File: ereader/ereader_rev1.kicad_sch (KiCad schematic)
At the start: 0 parts

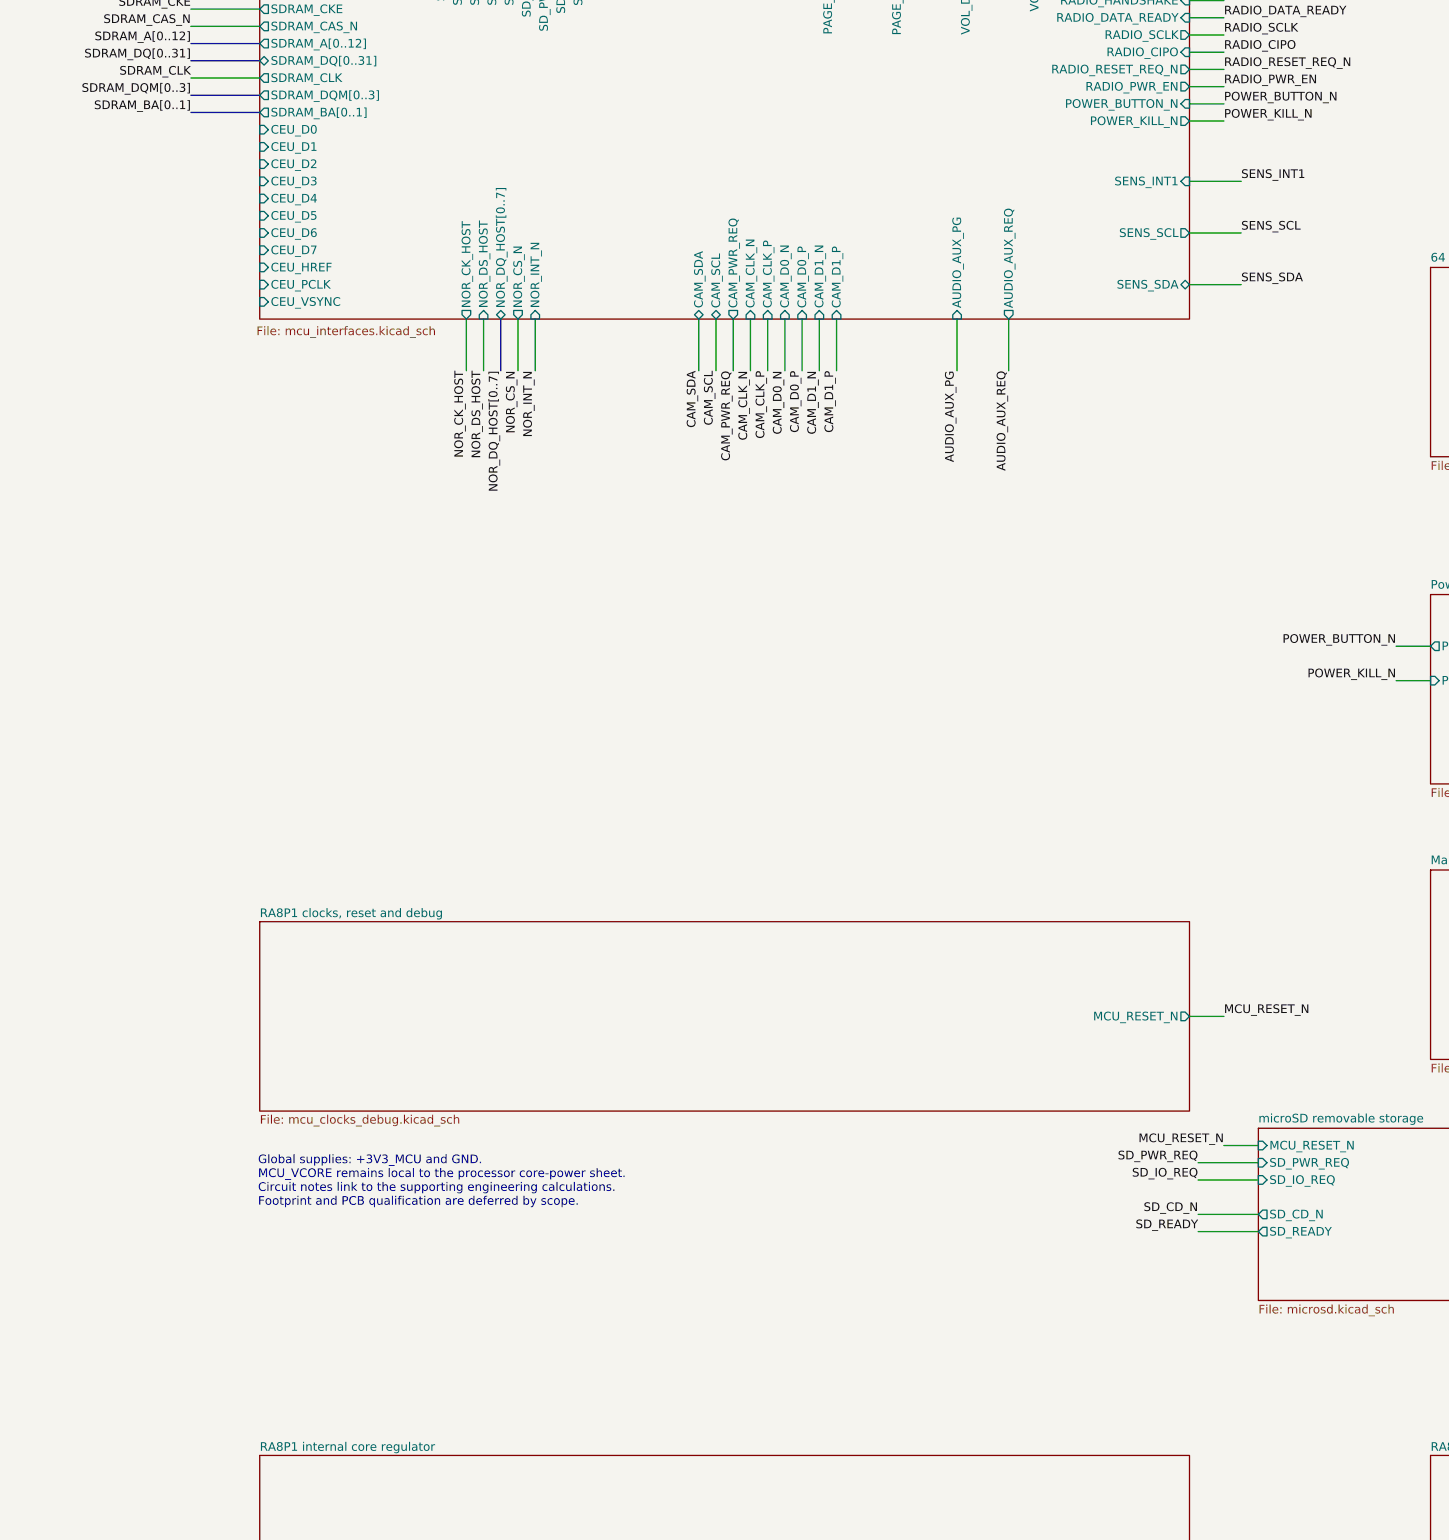
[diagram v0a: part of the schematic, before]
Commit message: Add buffered SCI4 NAND storage schematic
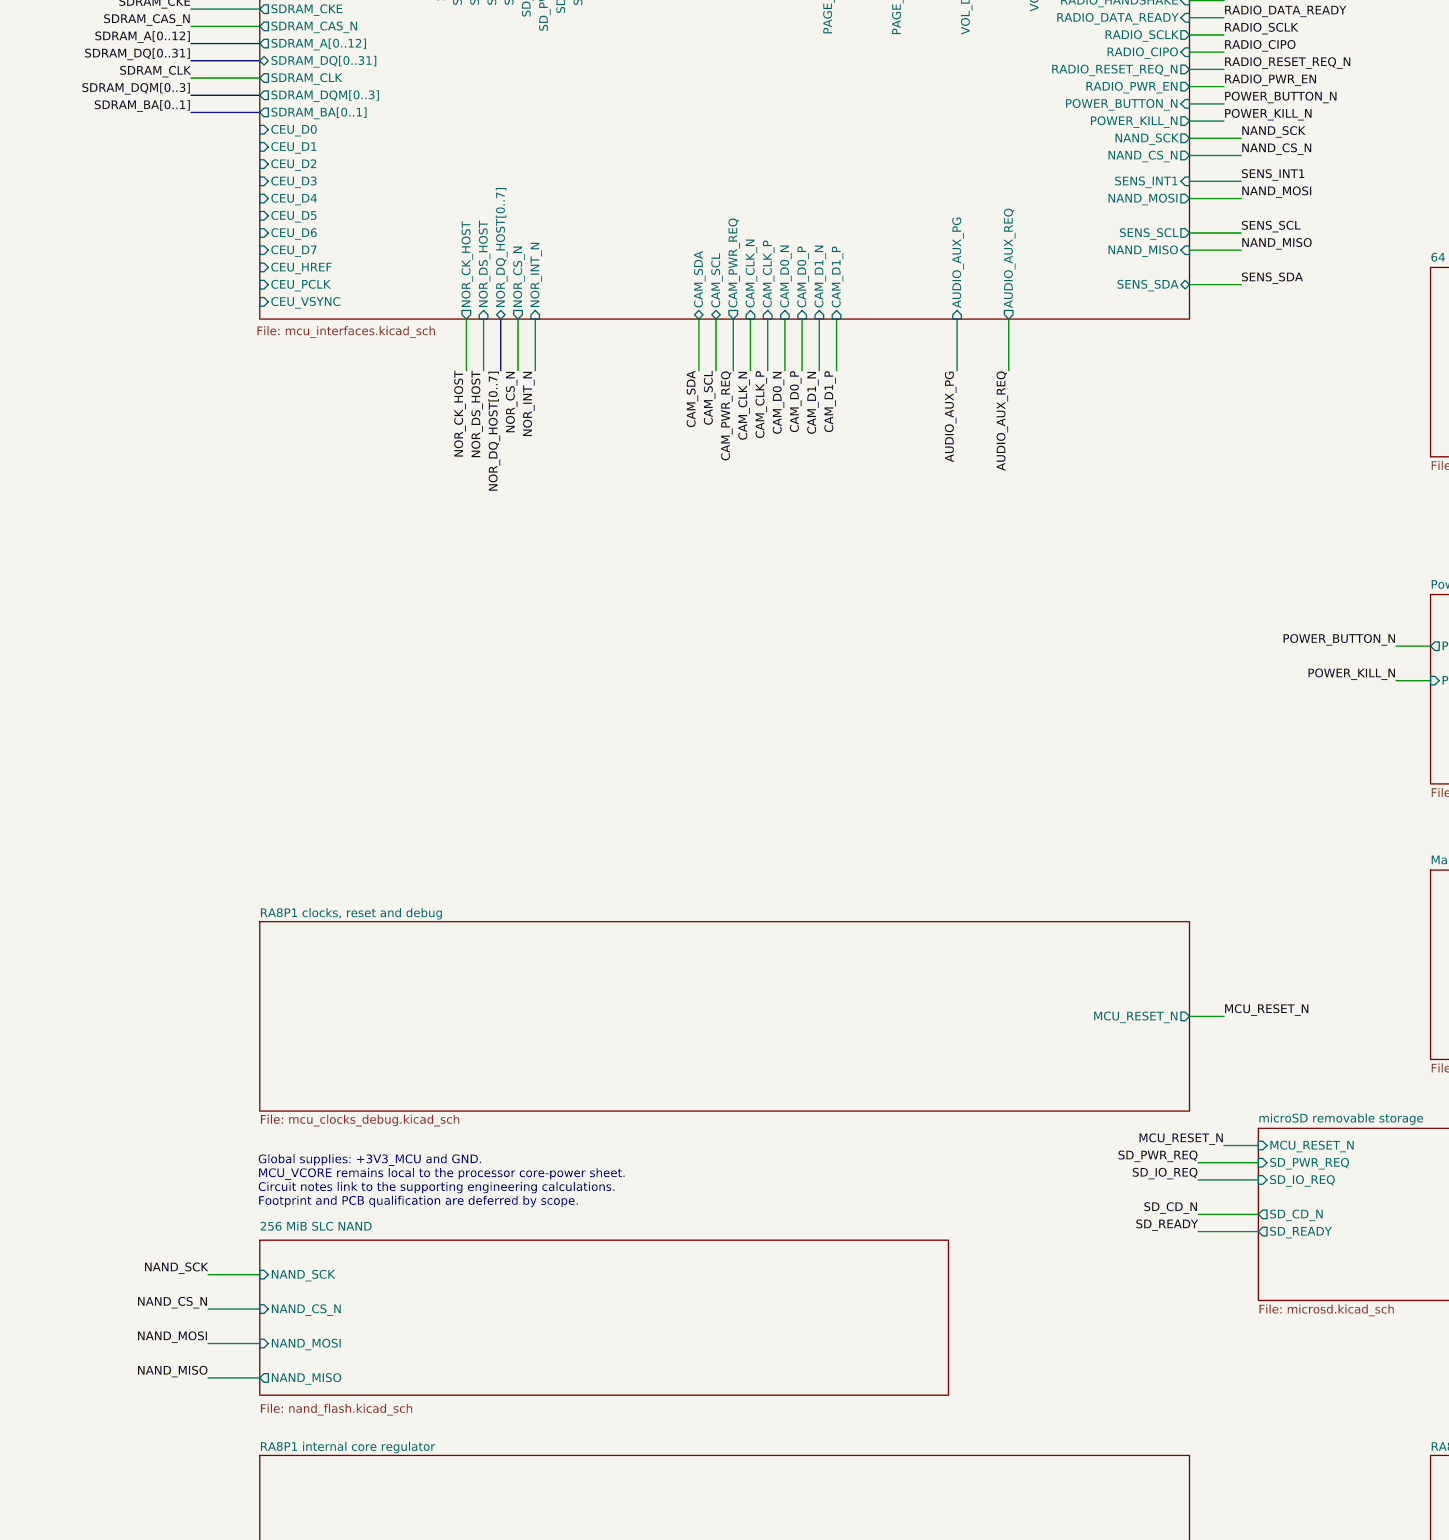
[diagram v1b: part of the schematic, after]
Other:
- added sheet 256 MiB SLC NAND (nand_flash.kicad_sch)
- sheet RA8P1 IO allocation ports: added NAND_CS_N, NAND_MISO, NAND_MOSI, NAND_SCK; removed none
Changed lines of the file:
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@@
 			)
 		)
-	)
+	(pin "NAND_SCK" output (at 199.39 106.68 0) (effects (font (size 1.27 1.27)) (justify right)))
+(pin "NAND_CS_N" output (at 199.39 109.22 0) (effects (font (size 1.27 1.27)) (justify right)))
+(pin "NAND_MOSI" output (at 199.39 115.57 0) (effects (font (size 1.27 1.27)) (justify right)))
+(pin "NAND_MISO" input (at 199.39 123.19 0) (effects (font (size 1.27 1.27)) (justify right)))
+)
 	(sheet
 		(at 209.55 252.73)
@@
 	)
 	(embedded_fonts no)
+(wire (pts (xy 199.39 106.68) (xy 207.01 106.68)) (stroke (width 0) (type default)))
+(label "NAND_SCK" (at 207.01 106.68 0) (effects (font (size 1.27 1.27)) (justify left bottom)))
+(wire (pts (xy 199.39 109.22) (xy 207.01 109.22)) (stroke (width 0) (type default)))
+(label "NAND_CS_N" (at 207.01 109.22 0) (effects (font (size 1.27 1.27)) (justify left bottom)))
+(wire (pts (xy 199.39 115.57) (xy 207.01 115.57)) (stroke (width 0) (type default)))
+(label "NAND_MOSI" (at 207.01 115.57 0) (effects (font (size 1.27 1.27)) (justify left bottom)))
+(wire (pts (xy 199.39 123.19) (xy 207.01 123.19)) (stroke (width 0) (type default)))
+(label "NAND_MISO" (at 207.01 123.19 0) (effects (font (size 1.27 1.27)) (justify left bottom)))
+(wire (pts (xy 62.23 274.32) (xy 54.61 274.32)) (stroke (width 0) (type default)))
+(label "NAND_SCK" (at 54.61 274.32 180) (effects (font (size 1.27 1.27)) (justify right bottom)))
+(wire (pts (xy 62.23 279.4) (xy 54.61 279.4)) (stroke (width 0) (type default)))
+(label "NAND_CS_N" (at 54.61 279.4 180) (effects (font (size 1.27 1.27)) (justify right bottom)))
+(wire (pts (xy 62.23 284.48) (xy 54.61 284.48)) (stroke (width 0) (type default)))
+(label "NAND_MOSI" (at 54.61 284.48 180) (effects (font (size 1.27 1.27)) (justify right bottom)))
+(wire (pts (xy 62.23 289.56) (xy 54.61 289.56)) (stroke (width 0) (type default)))
+(label "NAND_MISO" (at 54.61 289.56 180) (effects (font (size 1.27 1.27)) (justify right bottom)))
+(sheet (at 62.23 269.24) (size 101.6 22.86) (exclude_from_sim no) (in_bom yes) (on_board yes) (dnp no) (stroke (width 0.1524) (type solid)) (fill (color 0 0 0 0)) (property "Sheetname" "256 MiB SLC NAND" (at 62.23 267.97 0) (effects (font (size 1.27 1.27)) (justify left bottom)))(property "Sheetfile" "nand_flash.kicad_sch" (at 62.23 293.37 0) (effects (font (size 1.27 1.27)) (justify left top)))(pin "NAND_SCK" input (at 62.23 274.32 180) (effects (font (size 1.27 1.27)) (justify left)))(pin "NAND_CS_N" input (at 62.23 279.4 180) (effects (font (size 1.27 1.27)) (justify left)))(pin "NAND_MOSI" input (at 62.23 284.48 180) (effects (font (size 1.27 1.27)) (justify left)))(pin "NAND_MISO" output (at 62.23 289.56 180) (effects (font (size 1.27 1.27)) (justify left)))(instances (project "ereader_rev1" (path "/0586cc51-9c57-495b-a0c9-c29ba0d48166" (page "16")))))
 )

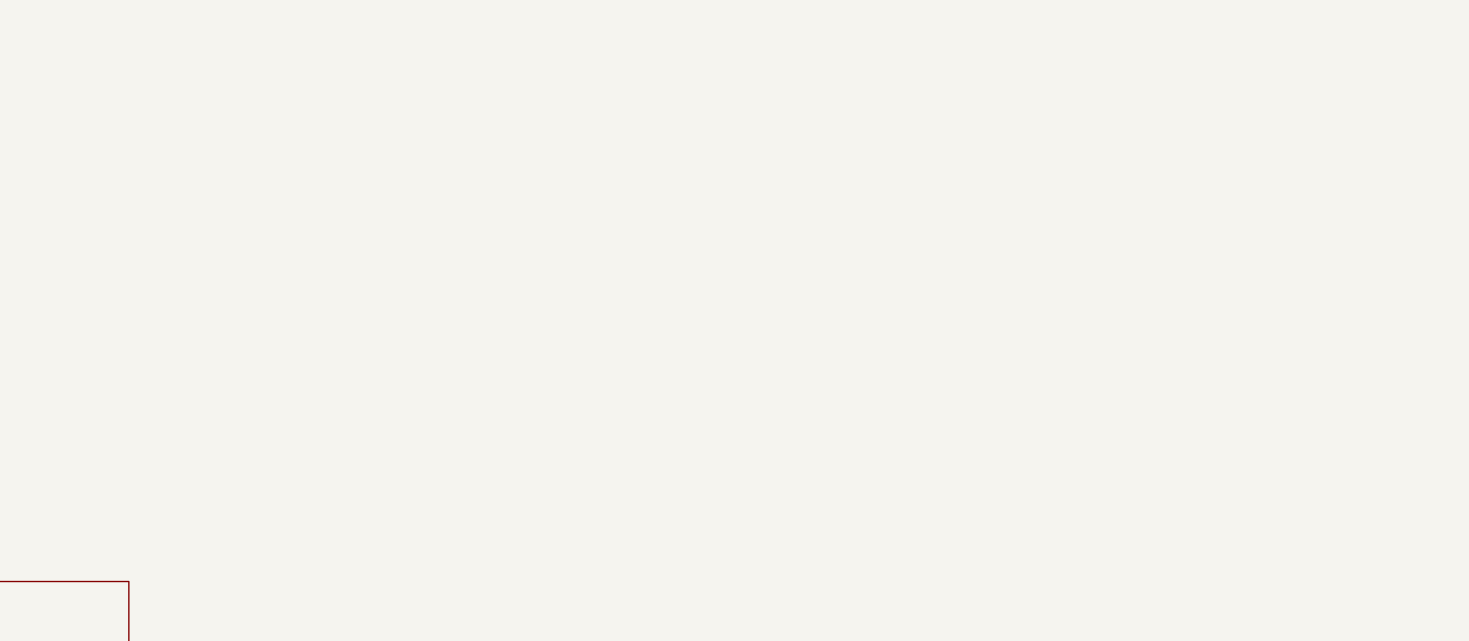
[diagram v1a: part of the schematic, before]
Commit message: Add isolated source-local AUX electrical draft and independent gates
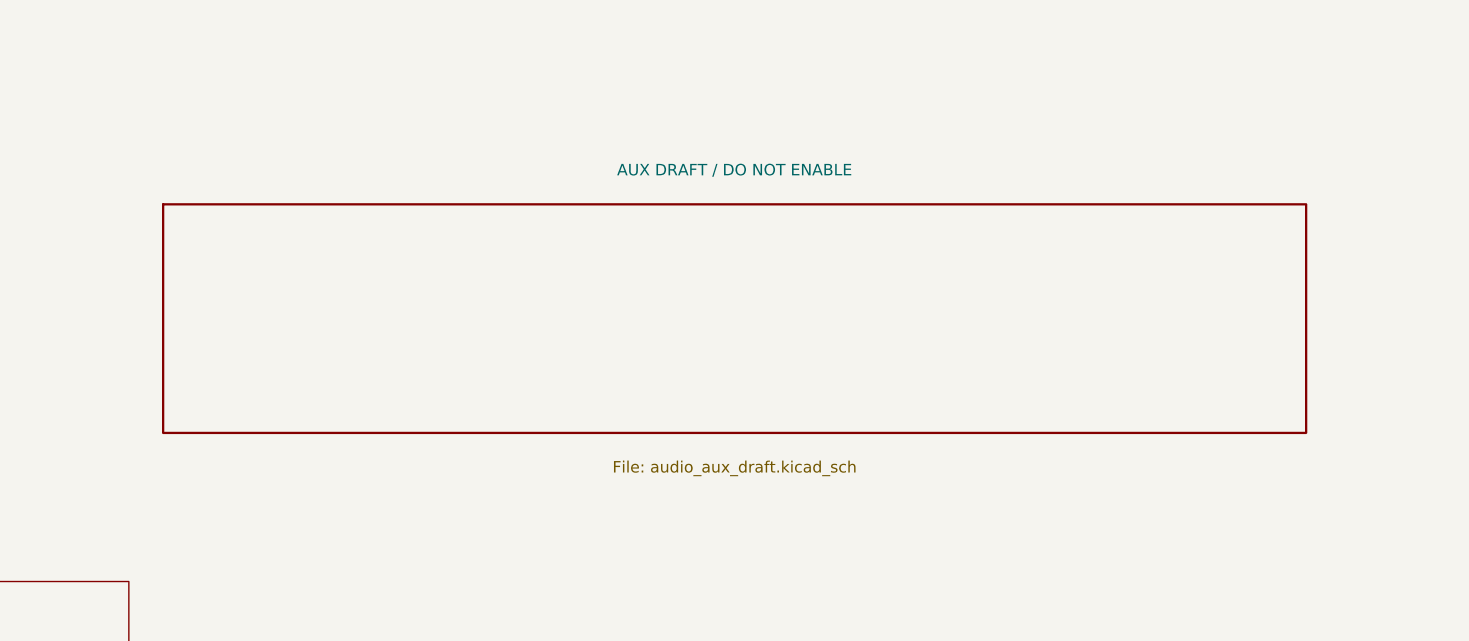
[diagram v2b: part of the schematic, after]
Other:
- added sheet AUX DRAFT / DO NOT ENABLE (audio_aux_draft.kicad_sch)
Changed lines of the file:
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@@
 (label "NAND_MISO" (at 54.61 289.56 180) (effects (font (size 1.27 1.27)) (justify right bottom)))
 (sheet (at 62.23 269.24) (size 101.6 22.86) (exclude_from_sim no) (in_bom yes) (on_board yes) (dnp no) (stroke (width 0.1524) (type solid)) (fill (color 0 0 0 0)) (property "Sheetname" "256 MiB SLC NAND" (at 62.23 267.97 0) (effects (font (size 1.27 1.27)) (justify left bottom)))(property "Sheetfile" "nand_flash.kicad_sch" (at 62.23 293.37 0) (effects (font (size 1.27 1.27)) (justify left top)))(pin "NAND_SCK" input (at 62.23 274.32 180) (effects (font (size 1.27 1.27)) (justify left)))(pin "NAND_CS_N" input (at 62.23 279.4 180) (effects (font (size 1.27 1.27)) (justify left)))(pin "NAND_MOSI" input (at 62.23 284.48 180) (effects (font (size 1.27 1.27)) (justify left)))(pin "NAND_MISO" output (at 62.23 289.56 180) (effects (font (size 1.27 1.27)) (justify left)))(instances (project "ereader_rev1" (path "/0586cc51-9c57-495b-a0c9-c29ba0d48166" (page "16")))))
+(sheet
+	(at 436.88 35.56)
+	(size 127 25.4)
+	(exclude_from_sim no)
+	(in_bom yes)
+	(on_board yes)
+	(dnp no)
+	(stroke (width 0.254) (type solid))
+	(fill (color 0 0 0 0))
+	(property "Sheetname" "AUX DRAFT / DO NOT ENABLE"
+		(at 500.38 31.75 0)
+		(effects
+			(font (size 1.27 1.27))
+		)
+	)
+	(property "Sheetfile" "audio_aux_draft.kicad_sch"
+		(at 500.38 64.77 0)
+		(effects
+			(font (size 1.27 1.27))
+		)
+	)
+	(instances
+		(project "ereader_rev1"
+			(path "/0586cc51-9c57-495b-a0c9-c29ba0d48166" (page "17"))
+		)
+		(project "audio_aux_draft"
+			(path "/4f02ca0f-19d6-5fbe-81f7-64747594a0bc" (page "1"))
+		)
+	)
 )
+)
